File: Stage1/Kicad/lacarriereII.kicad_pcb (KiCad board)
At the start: 2 copper layers, 92 x 92 mm, 75 parts, among them J1 USB_C_Receptacle_USB2.0, J2 Conn_02x06, J4 Conn_01x06_Pin, U1 PCA9557PW, U10 XC6206P132MR, U11 ESP32_WROVER, U13 BME280, U15 BME280, U2 BQ25171QWDRCRQ1, U3 CH340C, U4 UMH3N, U5 SIM800L-CORE, U6 FS8205, U7 HY2112, U8 TLV61070A, U9 XC6206P282MR

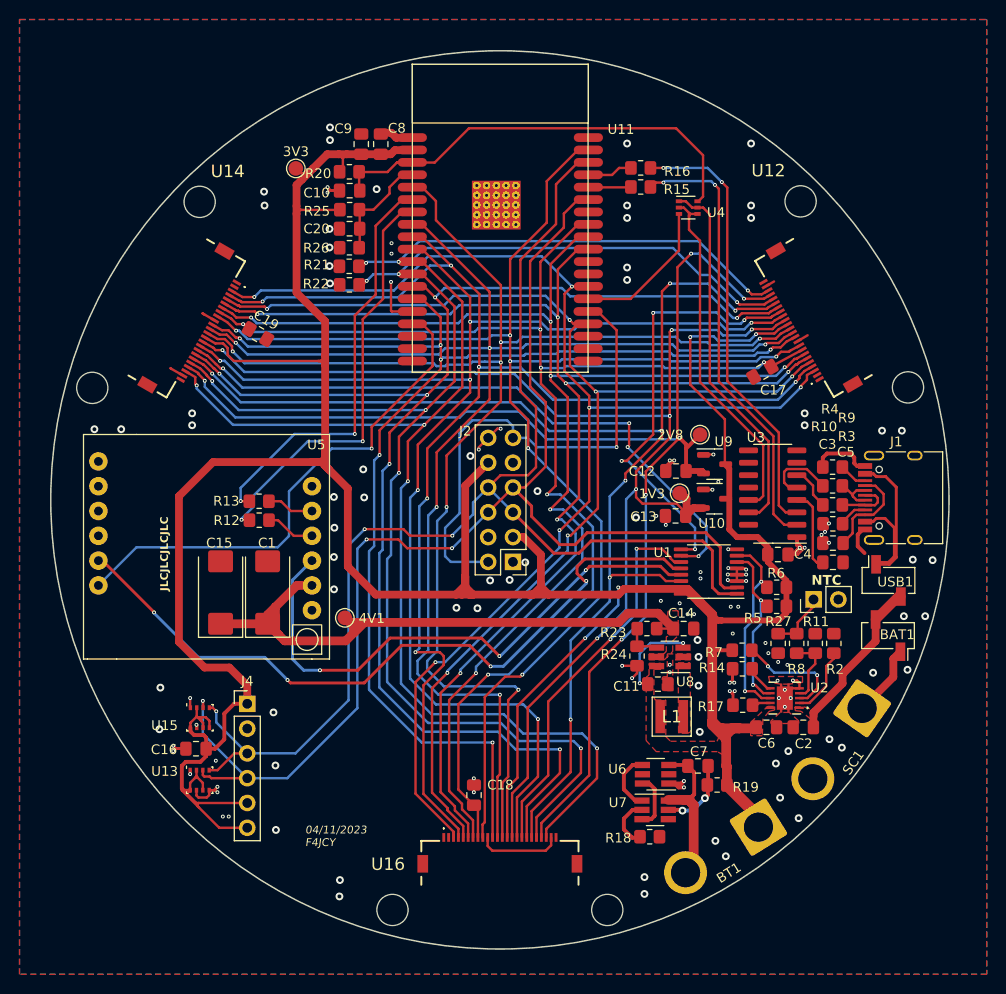
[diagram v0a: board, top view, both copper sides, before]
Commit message: [add] mounting holes + custom footprints lib
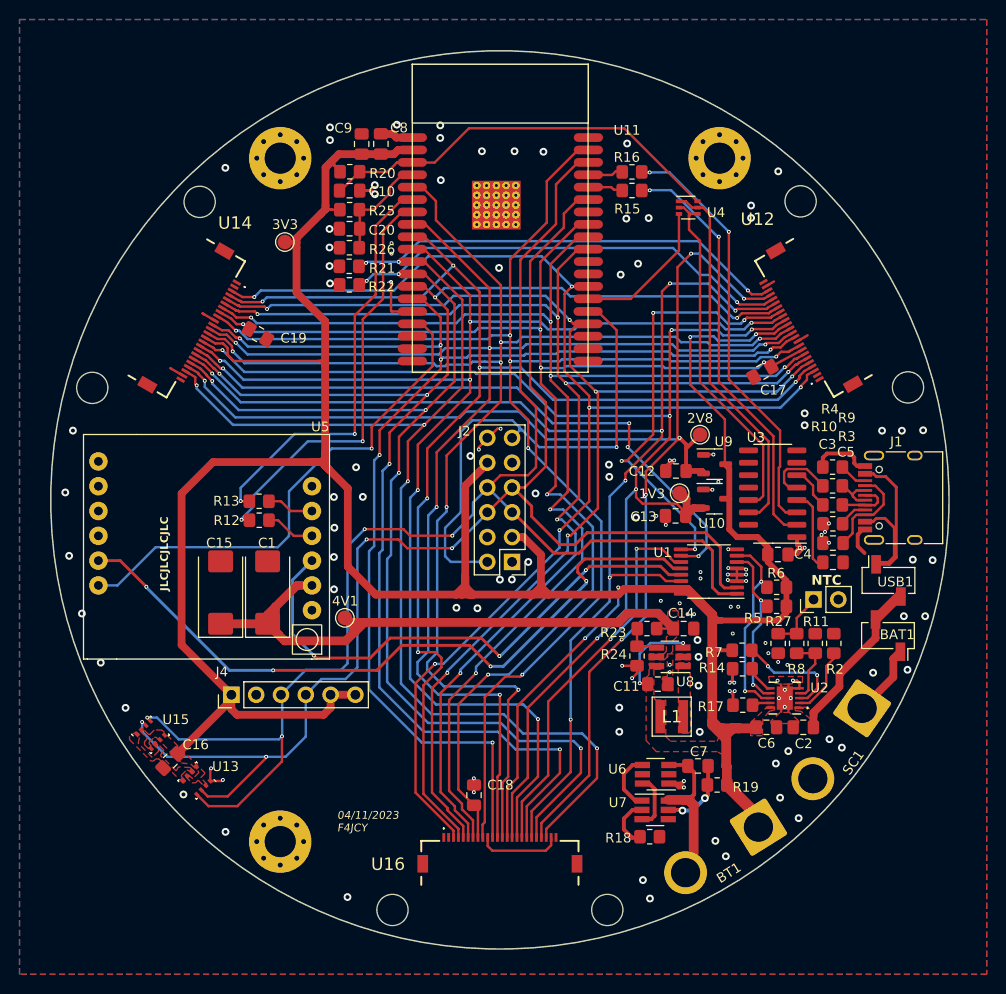
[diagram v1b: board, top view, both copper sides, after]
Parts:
- added H1: MountingHole_Pad, MountingHole:MountingHole_3.2mm_M3_Pad_Via, F.Cu at (77.5, 65.0)
- added H2: MountingHole_Pad, MountingHole:MountingHole_3.2mm_M3_Pad_Via, F.Cu at (122.5, 65.0)
- added H3: MountingHole_Pad, MountingHole:MountingHole_3.2mm_M3_Pad_Via, F.Cu at (77.5, 135.0)
- moved 3V3 7.62 mm to (78.0, 73.6)
- moved U15 5.33 mm to (64.2, 124.1), turned to 45 degrees
- moved C16 2.91 mm to (66.2, 126.7), turned to -135 degrees
- moved J4 1.87 mm to (72.5, 120.0), turned to 90 degrees
- moved R16 0.98 mm to (113.5, 66.4)
- moved R15 0.96 mm to (113.5, 68.3)
- moved U13 0.33 mm to (68.9, 128.8), turned to -135 degrees
- moved J2 0.09 mm to (100.0, 100.0)
- turned C10 to 0 degrees
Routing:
- net +3.3V: track 368.0 -> 343.0 mm
- net /I2C_SCL: track 132.0 -> 146.0 mm, vias 3 -> 4
- net /I2C_SDA: track 131.8 -> 137.8 mm, vias 3 -> 4
- net GND: track 87.9 -> 82.6 mm, vias 134 -> 135
- net /EN: track 45.1 -> 42.4 mm
- net Net-(U3-TXD): track 45.9 -> 43.3 mm
- net /GSM_RESET: track 57.5 -> 55.0 mm
- net Net-(U3-RXD): track 45.8 -> 44.1 mm
- net /GSM_SLEEP_MODE: track 74.8 -> 73.5 mm
- net /IO2: track 52.1 -> 53.0 mm
- net /RXD0: track 4.69 -> 4.00 mm
- net /D1: track 134.2 -> 133.7 mm
- net /TXD0: track 4.41 -> 3.90 mm

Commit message: [add] white border + stage1 image
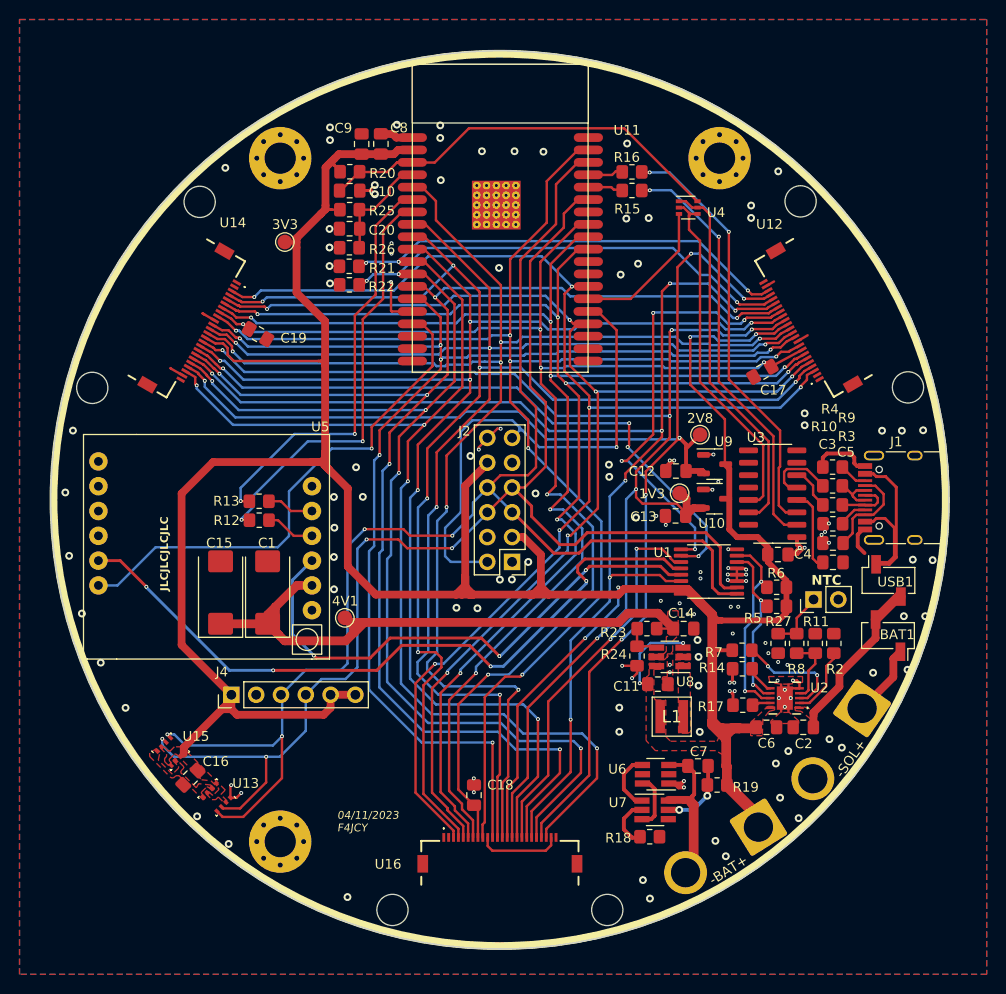
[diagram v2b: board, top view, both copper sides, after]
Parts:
- moved C16 2.68 mm to (68.3, 128.5)
- moved U15 2.68 mm to (66.3, 125.8)
- moved U13 2.68 mm to (71.0, 130.5)
- renumbered BT1 to -BAT+, SC1 to -SOL+
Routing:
- net /I2C_SDA: track 137.8 -> 134.2 mm
- net /I2C_SCL: track 146.0 -> 142.8 mm
- net +3.3V: track 343.0 -> 343.7 mm

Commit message: [update] Stage1 schematic after olli's review
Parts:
- removed the C20 at (84.6, 72.2)
- removed the R26 at (84.6, 74.2)
- added C11: NC(1u), Capacitor_SMD:C_0805_2012Metric_Pad1.18x1.45mm_HandSolder, F.Cu at (84.6, 74.1)
- added C13: 1u, Capacitor_SMD:C_0805_2012Metric_Pad1.18x1.45mm_HandSolder, F.Cu at (122.6, 93.5)
- added C14: 1u, Capacitor_SMD:C_0805_2012Metric_Pad1.18x1.45mm_HandSolder, F.Cu at (122.4, 102.4)
- added C21: 0.1u, Capacitor_SMD:C_0805_2012Metric_Pad1.18x1.45mm_HandSolder, F.Cu at (53.5, 132.2)
- added C23: 0.1u, Capacitor_SMD:C_0805_2012Metric_Pad1.18x1.45mm_HandSolder, F.Cu at (53.5, 135.2)
- added C24: 0.1u, Capacitor_SMD:C_0805_2012Metric_Pad1.18x1.45mm_HandSolder, F.Cu at (53.5, 138.2)
- added C3: 0.1u, Capacitor_SMD:C_0805_2012Metric_Pad1.18x1.45mm_HandSolder, F.Cu at (131.8, 99.4)
- added R1: 10k, Resistor_SMD:R_0805_2012Metric_Pad1.20x1.40mm_HandSolder, F.Cu at (104.5, 98.0)
- added R2: 10k, Resistor_SMD:R_0805_2012Metric_Pad1.20x1.40mm_HandSolder, F.Cu at (104.7, 99.8)
- added R24: 1M, Resistor_SMD:R_0805_2012Metric_Pad1.20x1.40mm_HandSolder, F.Cu at (84.6, 72.2)
- added U14: BME280, Package_LGA:Bosch_LGA-8_2.5x2.5mm_P0.65mm_ClockwisePinNumbering, F.Cu at (53.5, 126.9)
- added U16: BME280, Package_LGA:Bosch_LGA-8_2.5x2.5mm_P0.65mm_ClockwisePinNumbering, F.Cu at (57.3, 126.9)
- added U2: USBLC6-2SC6, Package_TO_SOT_SMD:SOT-23-6_Handsoldering, F.Cu at (131.8, 99.4)
- TH1: value NTC -> NC(NTC)
- moved 3V1 2.03 mm to (79.0, 71.8)
- turned R25 to 0 degrees
- turned R26 to 180 degrees
- renumbered 1V3 to 1V1, 2V8 to 2V1, 3V3 to 3V1, -BAT+ to BT1, C3 to C1, C11 to C12, C12 to C15, C13 to C16, C14 to C17, C15 to C18, C1 to C19, C16 to C20, C17 to C22, C18 to C25, C19 to C26, J4 to J3, R7 to R10, R8 to R11, R11 to R12, R14 to R13, R12 to R14, R13 to R15, R17 to R16, R15 to R17, R16 to R18, R18 to R19, R19 to R20, R20 to R21, R27 to R22, R25 to R23, R21 to R25, R22 to R26, R23 to R27, R24 to R28, R2 to R5, R9 to R6, R10 to R7, R5 to R8, R6 to R9, -SOL+ to SC1, U9 to U10, U10 to U11, U11 to U12, U12 to U13, U13 to U14, U14 to U15, U15 to U16, U16 to U17, U2 to U3, U3 to U4, U4 to U6, U6 to U7, U7 to U8, U8 to U9
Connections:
- J1 pad S1: unconnected-(J1-SHIELD-PadS1) -> GND
- J2 pad 11: unconnected-(J2-Pin_11-Pad11) -> /IO_EXT2
- J2 pad 12: /IO2 -> /IO_EXT1
- J2 pad 5: unconnected-(J2-Pin_5-Pad5) -> /IO_EXT2
- J2 pad 6: /IO2 -> /IO_EXT1
- R25 pad 1: /DVP_SDA -> +3.3V
- R25 pad 2: GND -> /DVP_SDA
- R26 pad 1: GND -> /DVP_SCL
- R26 pad 2: /DVP_SCL -> +3.3V
- R6 pad 2: Net-(U3-UD+) -> Net-(U2-I/O1_1)
- R7 pad 2: Net-(U3-UD-) -> Net-(U2-I/O2_1)
- U12 pad 23: /D3 -> /IO_EXT2
- U12 pad 24: /IO2 -> /D3
- U12 pad 25: /IO0 -> /IO0_AND_D5
- U12 pad 37: /D5 -> /IO_EXT1
- U13 pad 9: /D5 -> /IO0_AND_D5
- U15 pad 9: /D5 -> /IO0_AND_D5
- U17 pad 9: /D5 -> /IO0_AND_D5
- U4 pad 5: Net-(U3-UD+) -> Net-(U2-I/O1_2)
- U4 pad 6: Net-(U3-UD-) -> Net-(U2-I/O2_2)
- U6 pad 3: /IO0 -> /IO0_AND_D5
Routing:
- net (no net): track 0.00 -> 158.1 mm, vias 0 -> 6
- net /D5: track 145.6 -> 0.00 mm, vias 6 -> 0
- net /IO2: track 53.0 -> 0.00 mm, vias 1 -> 0
- net /D3: track 125.8 -> 178.8 mm, vias 6 -> 7
- net /IO0_AND_D5: track 0.00 -> 15.1 mm
- net /IO0: track 15.1 -> 0.00 mm
- net Net-(U3-UD+): track 7.31 -> 0.00 mm
- net +3.3V: track 343.7 -> 349.1 mm
- net Net-(U3-UD-): track 5.12 -> 0.00 mm
- net GND: track 82.6 -> 82.9 mm, vias 135 -> 133

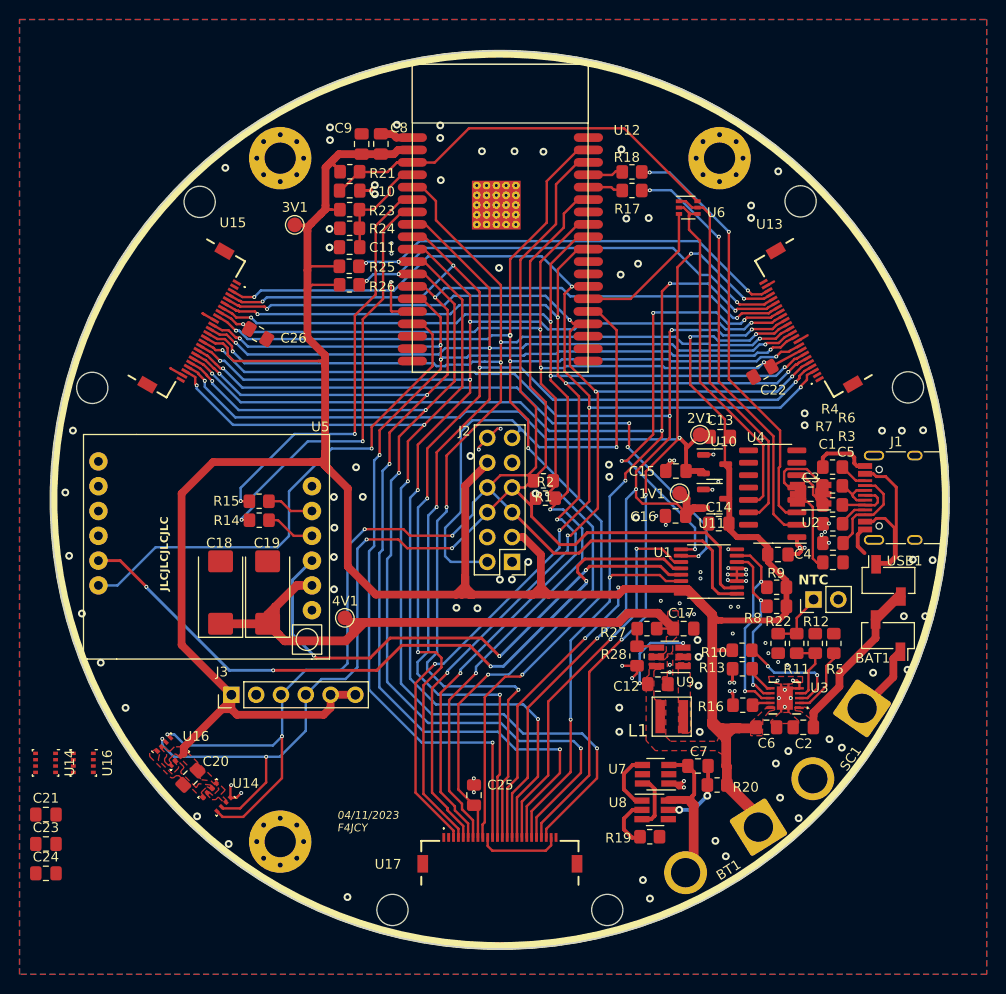
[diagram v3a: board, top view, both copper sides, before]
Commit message: [fix] a few mistakes on schematic ... ready to reroute!
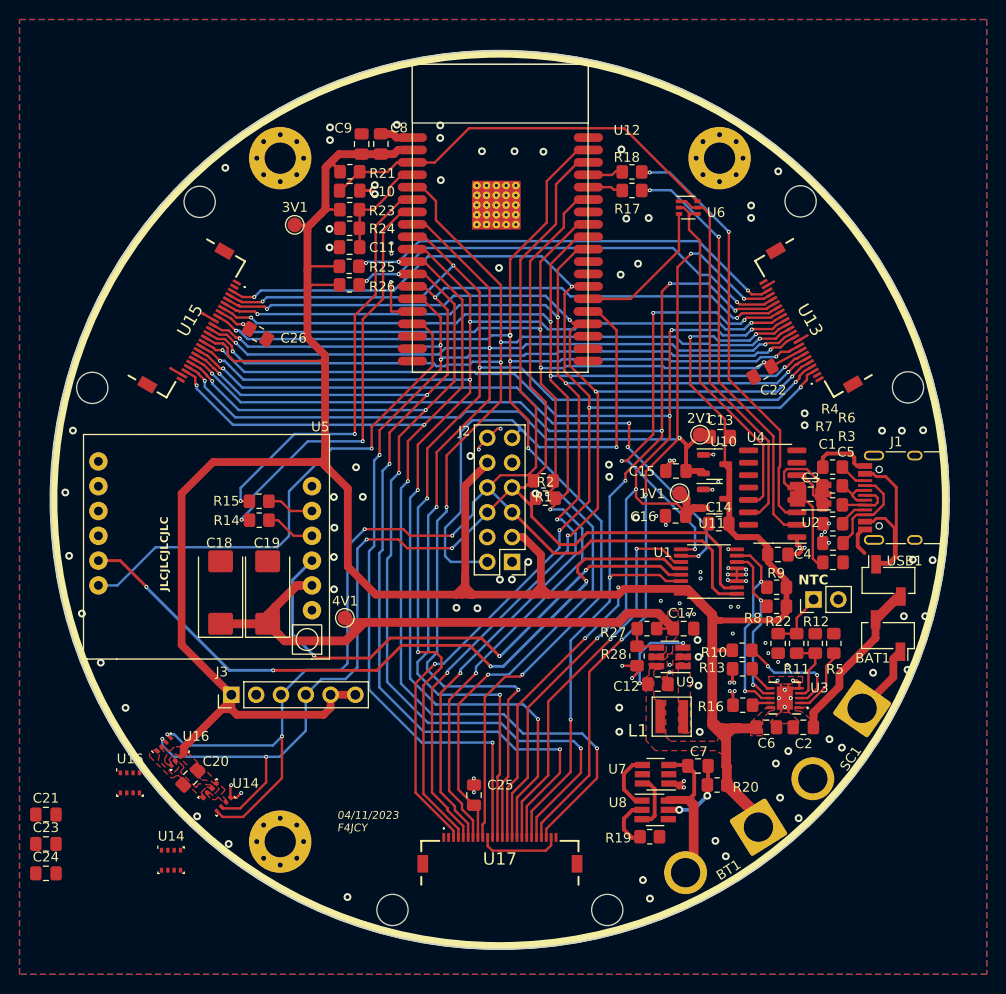
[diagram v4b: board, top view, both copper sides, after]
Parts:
- moved U14 16.3 mm to (66.3, 136.9), turned to 0 degrees
- moved U16 5.19 mm to (62.1, 129.0), turned to 0 degrees
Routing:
- net /IO_EXT1: track 0.00 -> 145.6 mm, vias 0 -> 6
- net (no net): track 158.1 -> 12.4 mm, vias 6 -> 0
- net /IO_EXT2: track 0.00 -> 125.8 mm, vias 0 -> 6
- net /D3: track 178.8 -> 53.0 mm, vias 7 -> 1

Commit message: [reroute] pcb board after oli's review
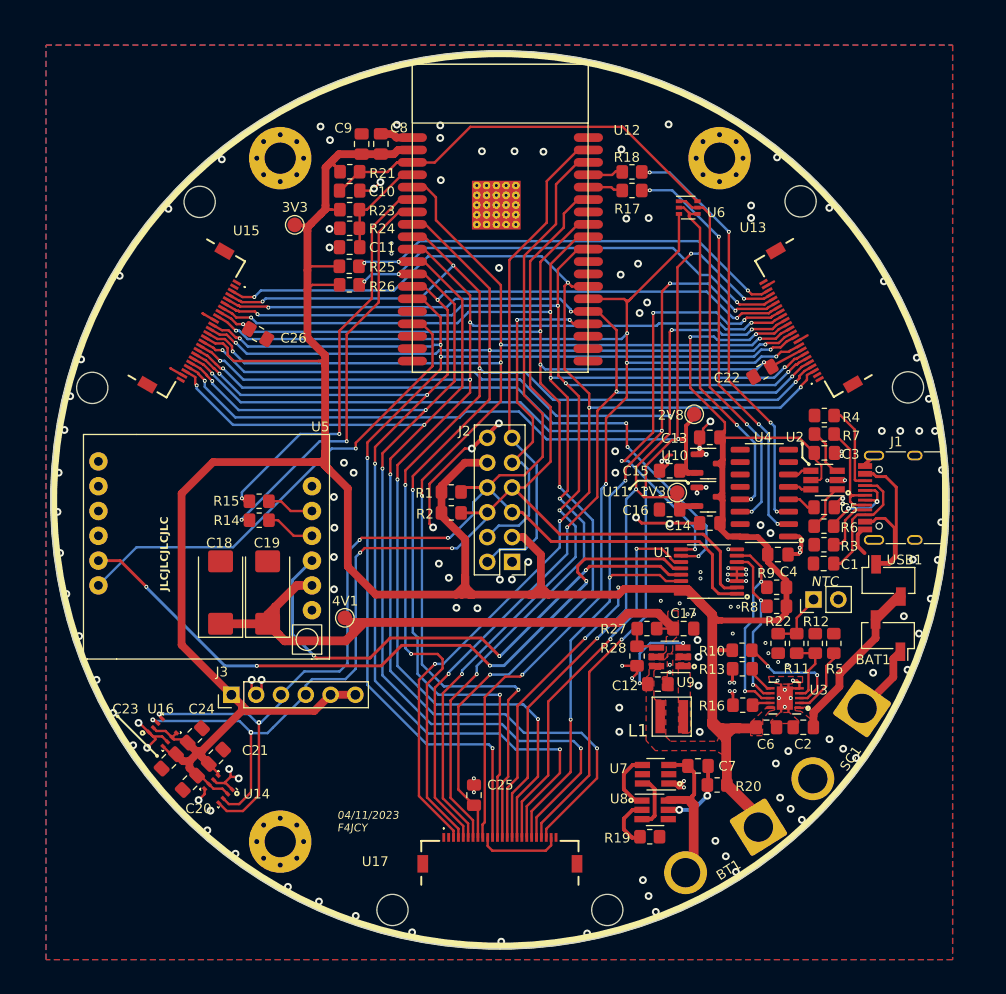
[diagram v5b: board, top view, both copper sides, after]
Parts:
- removed the U14 at (71.0, 130.5)
- removed the U16 at (66.3, 125.8)
- moved C24 20.8 mm to (68.8, 124.1), turned to 45 degrees
- moved C21 18.4 mm to (70.9, 126.3), turned to 45 degrees
- moved C23 15.2 mm to (66.1, 126.8), turned to -135 degrees
- moved R2 9.76 mm to (95.0, 101.3), turned to 180 degrees
- moved R1 9.51 mm to (95.0, 99.2), turned to 0 degrees
- moved U14 8.75 mm to (71.2, 129.6), turned to -135 degrees
- moved R7 7.30 mm to (133.2, 93.3)
- moved U16 6.15 mm to (65.5, 123.8), turned to 45 degrees
- moved C5 5.71 mm to (133.2, 100.8)
- moved R4 5.35 mm to (133.2, 91.4)
- moved C3 4.46 mm to (133.2, 95.2)
- moved R6 4.22 mm to (133.2, 102.7)
- moved R3 2.33 mm to (133.2, 104.6)
- moved C1 2.30 mm to (133.2, 106.5)
- moved 2V8 2.17 mm to (119.9, 91.2)
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- renumbered 1V1 to 1V3, 2V1 to 2V8, 3V1 to 3V3
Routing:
- net /IO0_AND_D5: track 15.1 -> 139.3 mm, vias 0 -> 6
- net /IO_EXT1: track 145.6 -> 50.9 mm, vias 6 -> 0
- net /IO_EXT2: track 125.8 -> 35.5 mm, vias 6 -> 2
- net /D3: track 53.0 -> 123.9 mm, vias 1 -> 6
- net +3.3V: track 349.1 -> 385.2 mm
- net GND: track 82.9 -> 108.6 mm, vias 133 -> 169
- net (no net): track 12.4 -> 0.00 mm
- net Net-(J1-CC2): track 2.91 -> 8.95 mm
- net Net-(J1-D--PadA7): track 5.61 -> 11.5 mm
- net Net-(U4-V3): track 8.30 -> 2.95 mm
- net Net-(U2-I/O2_1): track 0.00 -> 4.97 mm
- net Net-(J1-D+-PadA6): track 4.33 -> 9.19 mm, vias 0 -> 2
- net Net-(U2-I/O1_1): track 0.00 -> 4.80 mm
- net /GSM_RING: track 53.3 -> 49.7 mm
- net Net-(J1-SBU1): track 9.98 -> 12.9 mm
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
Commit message: [update] sourcing file + minors component placements on pcb
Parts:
- moved R27 0.14 mm to (115.1, 113.3)
- moved C17 0.11 mm to (118.8, 113.3)
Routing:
- net GND: track 108.6 -> 110.0 mm, vias 169 -> 186
- net +3.3V: track 385.2 -> 385.9 mm
- net /IO_EXT2: track 35.5 -> 36.0 mm
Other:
- board text added: "Lacarriere Stage 1"
